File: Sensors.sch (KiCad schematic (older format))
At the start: 39 parts, among them CN3 502351-0400, CN4 502351-0400, U10 MPXV4006GP, U11 MPXV4006DP, U12 TLV2333IDR, U17 MPXV4006GP

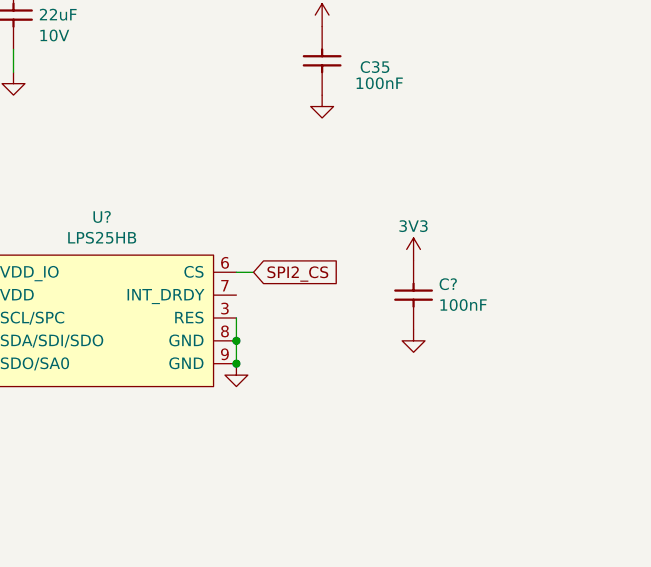
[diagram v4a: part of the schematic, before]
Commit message: SPI from FPGA to MCU and pressure sensor pins changed
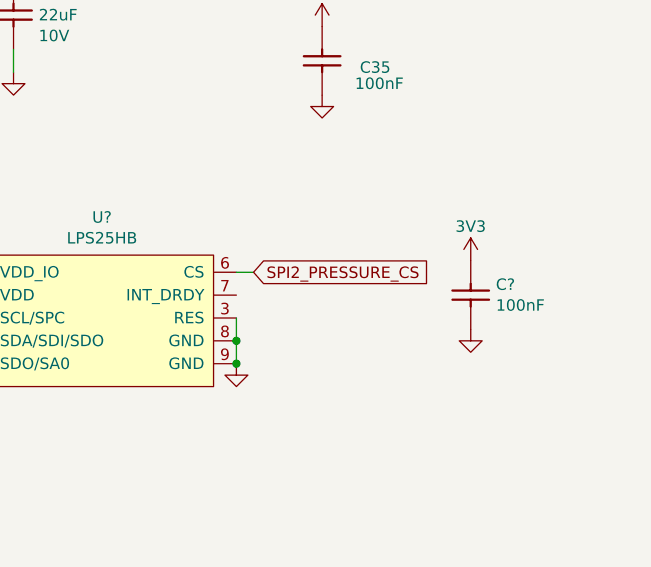
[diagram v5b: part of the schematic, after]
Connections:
- net SPI2_CS renamed SPI2_PRESSURE_CS
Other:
- moved on the sheet: C?
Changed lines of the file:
@@
 L OpenVent:3V3 #3V3_?
 U 1 1 602FA2B5
-P 10300 4300
+P 10550 4300
 AR Path="/5F988182/602FA2B5" Ref="#3V3_?"  Part="1"
 AR Path="/5F8F3873/602FA2B5" Ref="#3V3_?"  Part="1"
-F 0 "#3V3_?" H 10300 4300 20  0001 C CNN
-F 1 "3V3" H 10300 4450 50  0000 C CNN
-F 2 "" H 10300 4300 70  0001 C CNN
-F 3 "" H 10300 4300 70  0001 C CNN
-	1    10300 4300
+F 0 "#3V3_?" H 10550 4300 20  0001 C CNN
+F 1 "3V3" H 10550 4450 50  0000 C CNN
+F 2 "" H 10550 4300 70  0001 C CNN
+F 3 "" H 10550 4300 70  0001 C CNN
+	1    10550 4300
 	1    0    0    -1
 $EndComp
@@
 L OpenVent:100nF_0603_Ceramic_Capacitor,_10%,_X7R,_25V C?
 U 1 1 602FA2BE
-P 10400 4400
-F 0 "C?" V 10404 4410 50  0000 L CNN
-F 1 "100nF_0603_Ceramic_Capacitor,_10%,_X7R,_25V" H 10400 4400 50  0001 C CNN
-F 2 "" H 10400 4400 50  0001 C CNN
-F 3 "" H 10400 4400 50  0001 C CNN
-F 4 "100nF" V 10495 4410 50  0000 L CNN "Val"
-F 5 "25V" H 10400 4400 50  0001 C CNN "Voltage"
-F 6 "10%" H 10400 4400 50  0001 C CNN "Tolerance"
-	1    10400 4400
+P 10650 4400
+F 0 "C?" V 10654 4410 50  0000 L CNN
+F 1 "100nF_0603_Ceramic_Capacitor,_10%,_X7R,_25V" H 10650 4400 50  0001 C CNN
+F 2 "" H 10650 4400 50  0001 C CNN
+F 3 "" H 10650 4400 50  0001 C CNN
+F 4 "100nF" V 10745 4410 50  0000 L CNN "Val"
+F 5 "25V" H 10650 4400 50  0001 C CNN "Voltage"
+F 6 "10%" H 10650 4400 50  0001 C CNN "Tolerance"
+	1    10650 4400
 	0    1    1    0
 $EndComp
@@
 L OpenVent:GND #GND_?
 U 1 1 602FA2C4
-P 10300 4600
-F 0 "#GND_?" H 10300 4600 20  0001 C CNN
-F 1 "GND" H 10300 4530 50  0001 C CNN
-F 2 "" H 10300 4600 70  0000 C CNN
-F 3 "" H 10300 4600 70  0000 C CNN
-	1    10300 4600
+P 10550 4600
+F 0 "#GND_?" H 10550 4600 20  0001 C CNN
+F 1 "GND" H 10550 4530 50  0001 C CNN
+F 2 "" H 10550 4600 70  0000 C CNN
+F 3 "" H 10550 4600 70  0000 C CNN
+	1    10550 4600
 	1    0    0    -1
 $EndComp
@@
 Connection ~ 9525 4650
 Text GLabel 9600 4350 2    50   Input ~ 0
-SPI2_CS
+SPI2_PRESSURE_CS
 Text GLabel 8200 4750 0    50   Output ~ 0
 SPI2_MISO

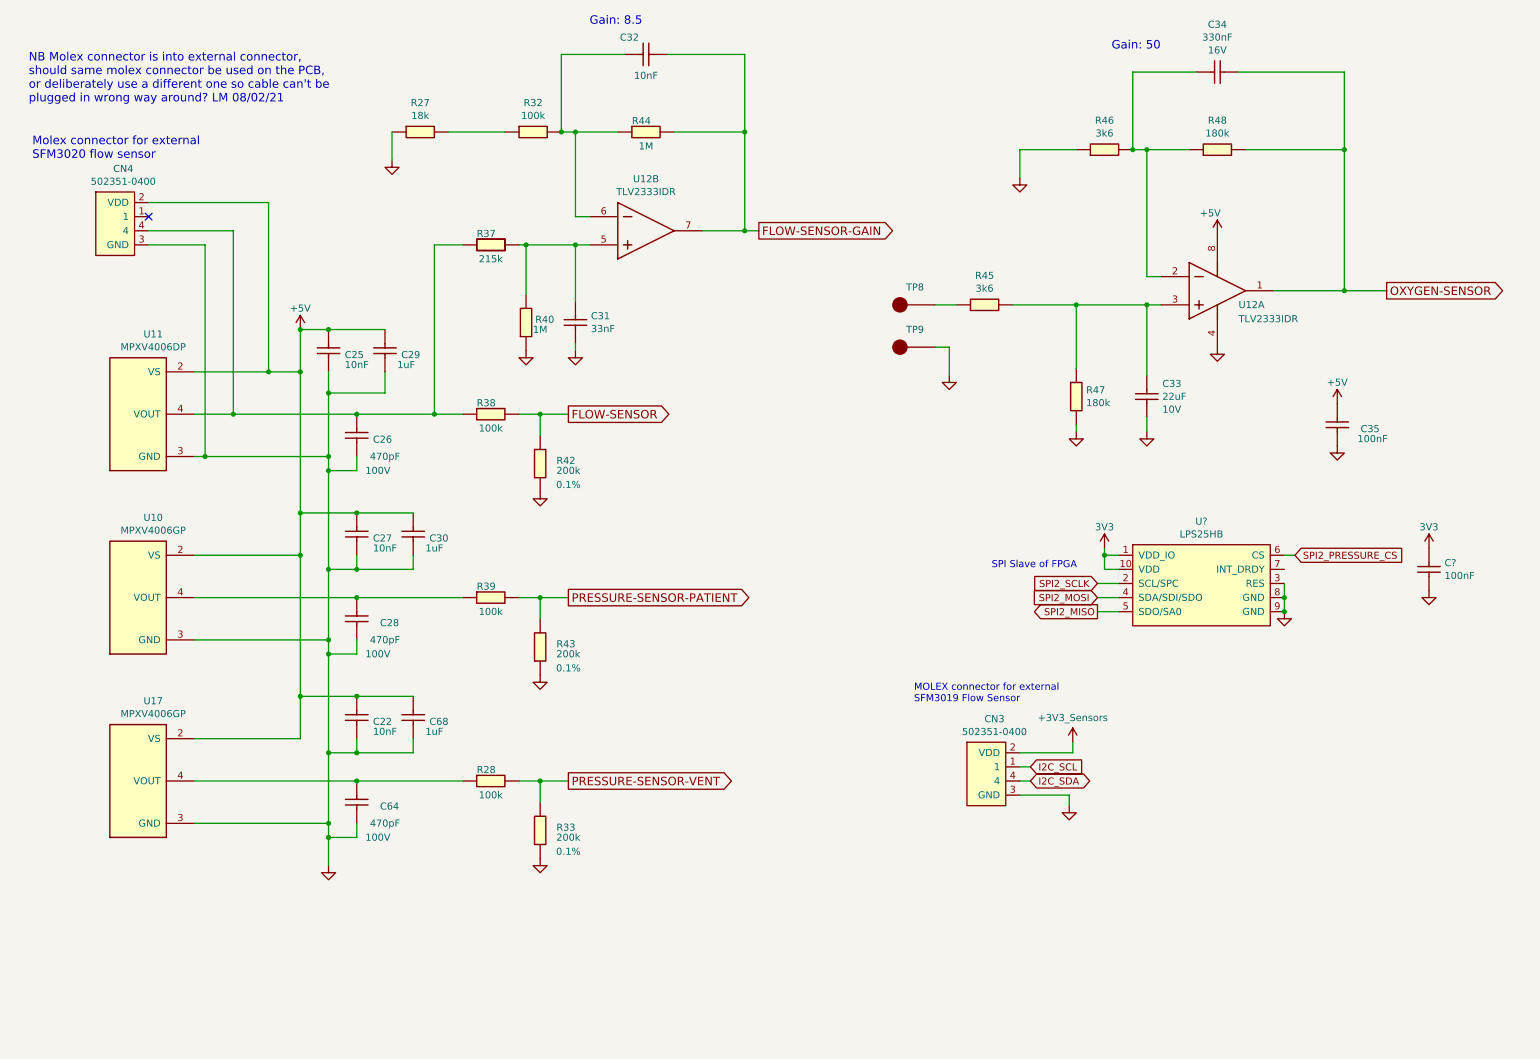
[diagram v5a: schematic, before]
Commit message: Sensor page edited, notes added and connectors swapped to 4way SMD
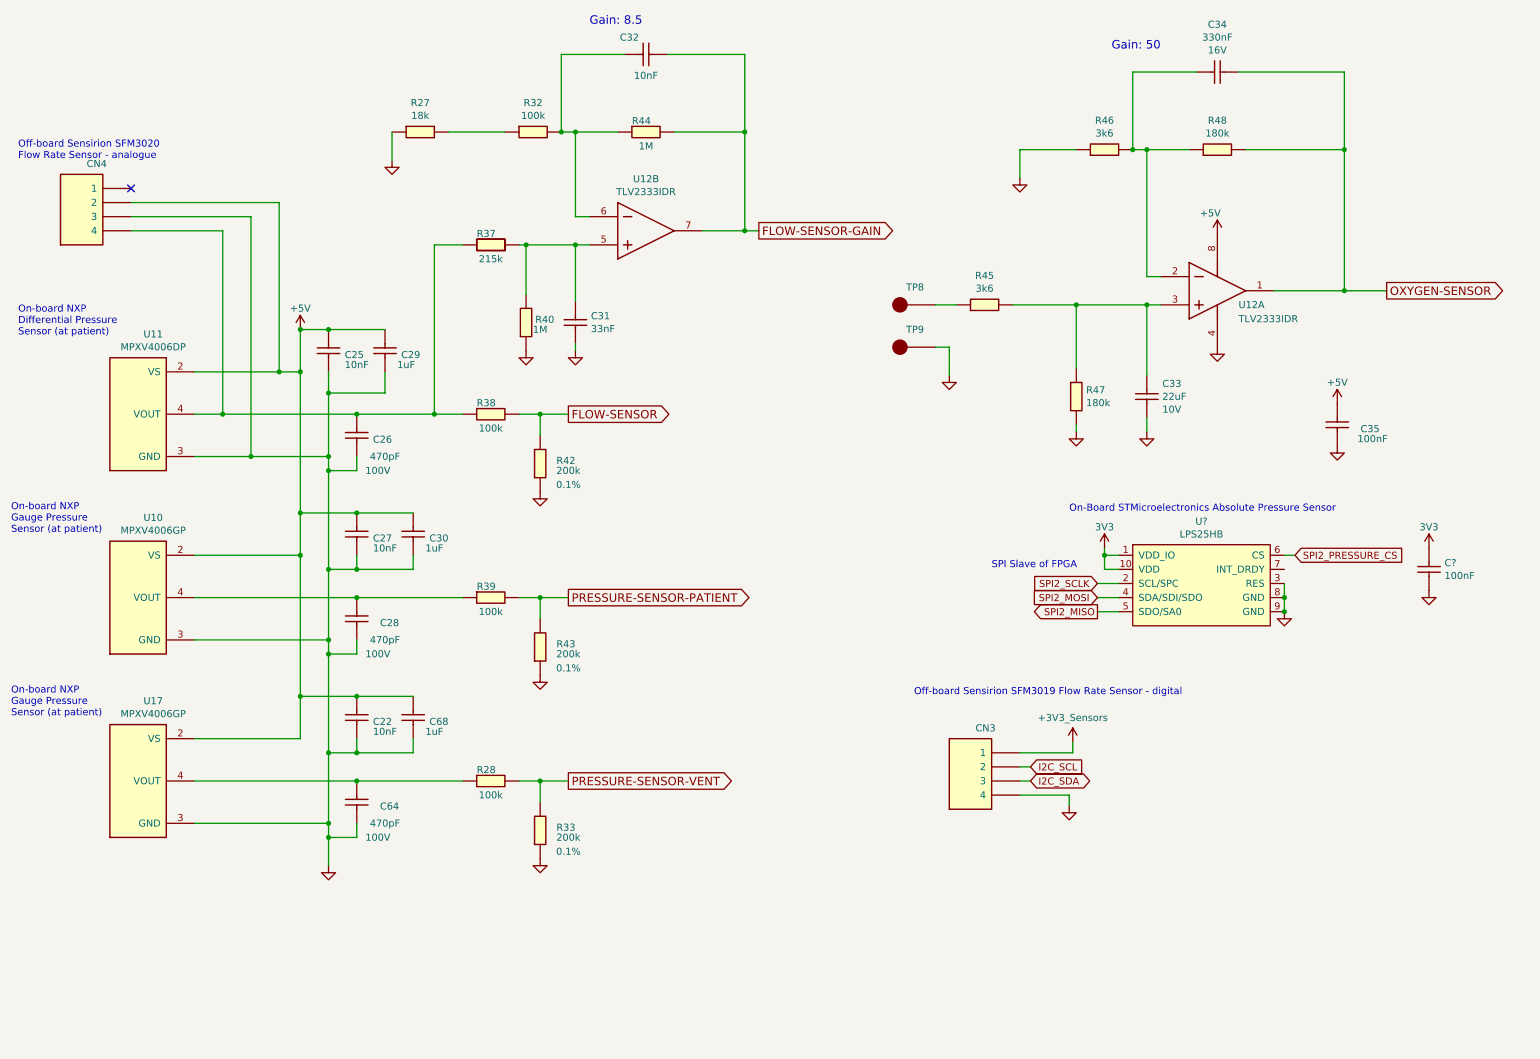
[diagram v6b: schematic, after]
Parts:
- removed CN3, CN4: 502351-0400, symbol OpenVent:502351-0400
- added CN3, CN4: CONN_HEADER_SMD_4POS_2MM, symbol OpenVent:CONN_HEADER_SMD_4POS_2MM
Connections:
- net +3.3V: now also CN3.1
- net +5V: now also CN4.2
- net GND: now also CN3.4, CN4.3
- net I2C_SCL: now also CN3.2
- net I2C_SDA: now also CN3.3
- net at C26.2, R37.1, R38.1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: now also CN4.4
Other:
- note added: "Off-board Sensirion SFM3019 Flow Rate Sensor - digital"
- note added: "Off-board Sensirion SFM3020\nFlow Rate Sensor - analogue"
- note added: "On-Board STMicroelectronics Absolute Pressure Sensor"
- note added: "On-board NXP\nDifferential Pressure\nSensor (at patient)"
- note added: "On-board NXP\nGauge Pressure\nSensor (at patient)"
- note removed: "MOLEX connector for external\nSFM3019 Flow Sensor"
- note removed: "Molex connector for external\nSFM3020 flow sensor"
- note removed: "NB Molex connector is into external connector,\nshould same molex connector be used on the PCB,\nor deliberately use a different one so cable can't be\nplugged in wrong way around? LM 08/02/21"
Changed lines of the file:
@@
 	1    0    0    -1
 $EndComp
-Text Notes 650  1550 0    60   ~ 0
-Molex connector for external\nSFM3020 flow sensor
 $Comp
 L OpenVent:GND #GND_031
@@
 	1    0    0    -1
 $EndComp
-NoConn ~ 1475 1950
+NoConn ~ 1350 1750
 Wire Wire Line
 	8550 2575 8550 3075
@@
 Connection ~ 2750 5750
 $Comp
-L OpenVent:502351-0400 CN3
-U 1 1 6027899F
-P 7425 5525
-F 0 "CN3" H 7470 5540 50  0000 C CNN
-F 1 "502351-0400" H 7470 5449 50  0000 C CNN
-F 2 "" H 7425 5525 50  0001 C CNN
-F 3 "" H 7425 5525 50  0001 C CNN
-	1    7425 5525
-	1    0    0    -1
-$EndComp
-$Comp
 L OpenVent:+3V3_Sensors #PWR03
 U 1 1 6027FA4F
@@
 Wire Wire Line
 	7650 5950 7725 5950
-Text Notes 6900 5400 0    50   ~ 0
-MOLEX connector for external\nSFM3019 Flow Sensor
-$Comp
-L OpenVent:502351-0400 CN4
-U 1 1 602C9734
-P 1250 1625
-F 0 "CN4" H 1295 1640 50  0000 C CNN
-F 1 "502351-0400" H 1295 1549 50  0000 C CNN
-F 2 "" H 1250 1625 50  0001 C CNN
-F 3 "" H 1250 1625 50  0001 C CNN
-	1    1250 1625
-	1    0    0    -1
-$EndComp
-Wire Wire Line
-	1800 3650 1875 3650
-Wire Wire Line
-	1800 3050 2325 3050
-Wire Wire Line
-	1800 3350 2075 3350
-Wire Wire Line
-	2325 3050 2325 1850
-Wire Wire Line
-	2325 1850 1475 1850
-Connection ~ 2325 3050
-Wire Wire Line
-	2325 3050 2550 3050
-Wire Wire Line
-	2075 3350 2075 2050
-Wire Wire Line
-	2075 2050 1475 2050
-Connection ~ 2075 3350
-Wire Wire Line
-	2075 3350 2950 3350
-Wire Wire Line
-	1475 2150 1875 2150
-Wire Wire Line
-	1875 2150 1875 3650
-Connection ~ 1875 3650
-Wire Wire Line
-	1875 3650 2750 3650
-Text Notes 625  1150 0    60   ~ 0
-NB Molex connector is into external connector,\nshould same molex connector be used on the PCB,\nor deliberately use a different one so cable can't be\nplugged in wrong way around? LM 08/02/21
 $Comp
 L OpenVent:LPS25HB U?
@@
 Text Notes 7450 4450 0    50   ~ 0
 SPI Slave of FPGA
+Text Notes 8000 4050 0    50   ~ 0
+On-Board STMicroelectronics Absolute Pressure Sensor
+Text Notes 550  2800 0    50   ~ 0
+On-board NXP\nDifferential Pressure\nSensor (at patient)
+Text Notes 500  4200 0    50   ~ 0
+On-board NXP\nGauge Pressure\nSensor (at patient)
+Text Notes 500  5500 0    50   ~ 0
+On-board NXP\nGauge Pressure\nSensor (at patient)
+Text Notes 6900 5350 0    50   ~ 0
+Off-board Sensirion SFM3019 Flow Rate Sensor - digital
+Text Notes 550  1550 0    50   ~ 0
+Off-board Sensirion SFM3020\nFlow Rate Sensor - analogue
+$Comp
+L OpenVent:CONN_HEADER_SMD_4POS_2MM CN3
+U 1 1 603F84CE
+P 7650 6050
+F 0 "CN3" H 7893 6525 50  0000 C CNN
+F 1 "CONN_HEADER_SMD_4POS_2MM" H 7950 5850 50  0001 C CNN
+F 2 "" H 7850 6450 50  0001 C CNN
+F 3 "" H 7850 6450 50  0001 C CNN
+	1    7650 6050
+	-1   0    0    -1
+$EndComp
+$Comp
+L OpenVent:CONN_HEADER_SMD_4POS_2MM CN4
+U 1 1 603F977D
+P 1350 2050
+F 0 "CN4" H 1593 2525 50  0000 C CNN
+F 1 "CONN_HEADER_SMD_4POS_2MM" H 1650 1850 50  0001 C CNN
+F 2 "" H 1550 2450 50  0001 C CNN
+F 3 "" H 1550 2450 50  0001 C CNN
+	1    1350 2050
+	-1   0    0    -1
+$EndComp
+Wire Wire Line
+	2000 2050 2000 3350
+Wire Wire Line
+	2400 1850 2400 3050
+Connection ~ 2400 3050
+Wire Wire Line
+	2400 3050 2550 3050
+Wire Wire Line
+	1800 3050 2400 3050
+Wire Wire Line
+	1350 1850 2400 1850
+Wire Wire Line
+	1800 3650 2200 3650
+Wire Wire Line
+	2200 3650 2200 1950
+Connection ~ 2200 3650
+Wire Wire Line
+	2200 3650 2750 3650
+Wire Wire Line
+	2200 1950 1350 1950
+Connection ~ 2000 3350
+Wire Wire Line
+	2000 3350 2950 3350
+Wire Wire Line
+	1800 3350 2000 3350
+Wire Wire Line
+	1350 2050 2000 2050
 $EndSCHEMATC

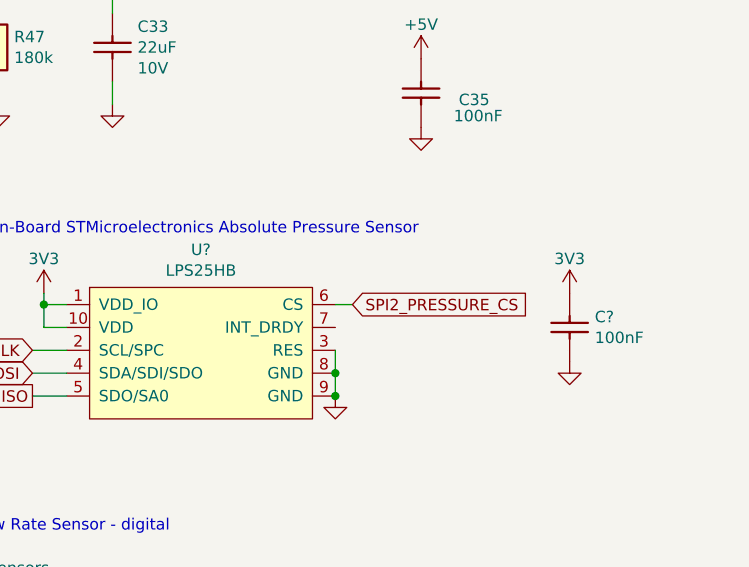
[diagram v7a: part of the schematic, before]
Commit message: Header 2x5 for FPGA was added to JTAG sheet
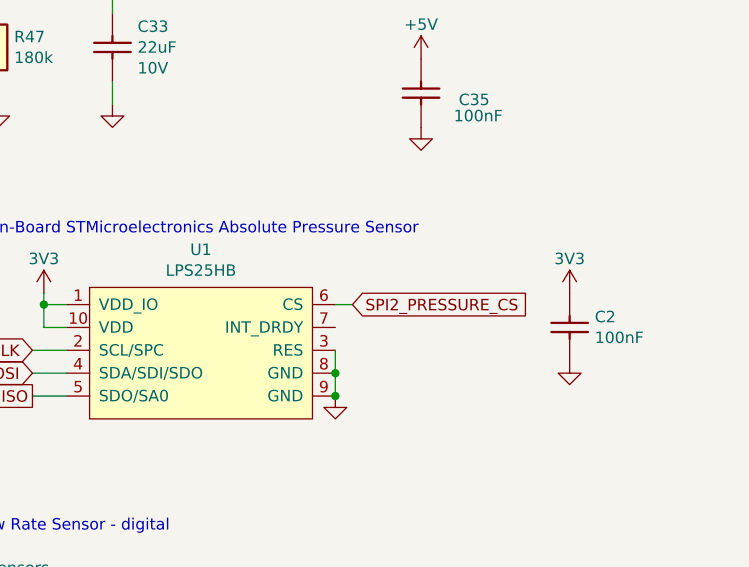
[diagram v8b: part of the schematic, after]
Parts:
- gave numbers to parts that had none: 2
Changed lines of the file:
@@
 	7650 5950 7725 5950
 $Comp
-L OpenVent:LPS25HB U?
+L OpenVent:LPS25HB U1
 U 1 1 602FA2A4
 P 8450 4350
-F 0 "U?" H 8937 4590 50  0000 C CNN
+F 0 "U1" H 8937 4590 50  0000 C CNN
 F 1 "LPS25HB" H 8937 4499 50  0000 C CNN
 F 2 "" H 8450 4350 50  0001 C CNN
@@
 P 8250 4300
 AR Path="/5F988182/602FA2AA" Ref="#3V3_?"  Part="1"
-AR Path="/5F8F3873/602FA2AA" Ref="#3V3_?"  Part="1"
-F 0 "#3V3_?" H 8250 4300 20  0001 C CNN
+AR Path="/5F8F3873/602FA2AA" Ref="#3V3_0101"  Part="1"
+F 0 "#3V3_0101" H 8250 4300 20  0001 C CNN
 F 1 "3V3" H 8250 4450 50  0000 C CNN
 F 2 "" H 8250 4300 70  0001 C CNN
@@
 P 10550 4300
 AR Path="/5F988182/602FA2B5" Ref="#3V3_?"  Part="1"
-AR Path="/5F8F3873/602FA2B5" Ref="#3V3_?"  Part="1"
-F 0 "#3V3_?" H 10550 4300 20  0001 C CNN
+AR Path="/5F8F3873/602FA2B5" Ref="#3V3_0102"  Part="1"
+F 0 "#3V3_0102" H 10550 4300 20  0001 C CNN
 F 1 "3V3" H 10550 4450 50  0000 C CNN
 F 2 "" H 10550 4300 70  0001 C CNN
@@
 $EndComp
 $Comp
-L OpenVent:100nF_0603_Ceramic_Capacitor,_10%,_X7R,_25V C?
+L OpenVent:100nF_0603_Ceramic_Capacitor,_10%,_X7R,_25V C2
 U 1 1 602FA2BE
 P 10650 4400
-F 0 "C?" V 10654 4410 50  0000 L CNN
+F 0 "C2" V 10654 4410 50  0000 L CNN
 F 1 "100nF_0603_Ceramic_Capacitor,_10%,_X7R,_25V" H 10650 4400 50  0001 C CNN
 F 2 "" H 10650 4400 50  0001 C CNN
@@
 $EndComp
 $Comp
-L OpenVent:GND #GND_?
+L OpenVent:GND #GND_0103
 U 1 1 602FA2C4
 P 10550 4600
-F 0 "#GND_?" H 10550 4600 20  0001 C CNN
+F 0 "#GND_0103" H 10550 4600 20  0001 C CNN
 F 1 "GND" H 10550 4530 50  0001 C CNN
 F 2 "" H 10550 4600 70  0000 C CNN
@@
 $EndComp
 $Comp
-L OpenVent:GND #GND_?
+L OpenVent:GND #GND_0104
 U 1 1 602FA2CA
 P 9525 4750
-F 0 "#GND_?" H 9525 4750 20  0001 C CNN
+F 0 "#GND_0104" H 9525 4750 20  0001 C CNN
 F 1 "GND" H 9525 4680 50  0001 C CNN
 F 2 "" H 9525 4750 70  0000 C CNN
